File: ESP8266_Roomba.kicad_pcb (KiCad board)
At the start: 2 copper layers, 100 x 30 mm, 68 parts, among them P1 USB_OTG, P2 UG_62864, P3 CONN_01X04, P4 CONN_01X02, P5 CONN_01X07, P6 CONN_01X02, Q1 DMC204010R, Q2 2N7002, Q4 2N7002, Q5 2N7002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

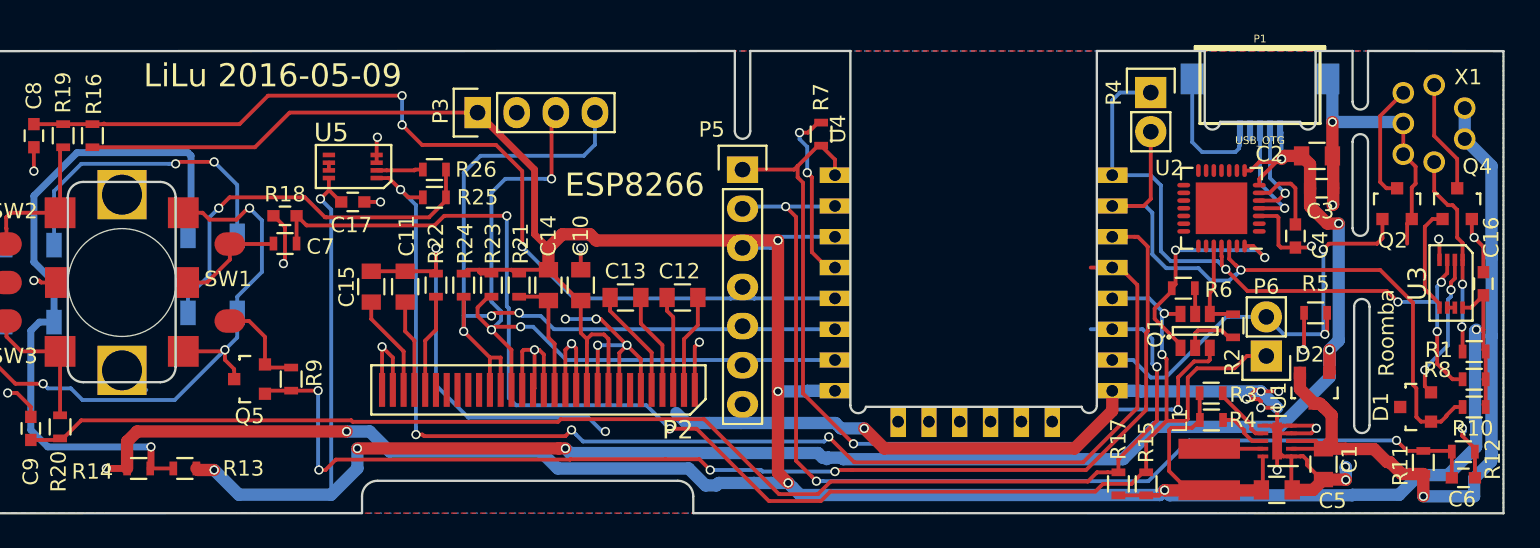
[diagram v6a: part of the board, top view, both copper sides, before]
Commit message: Revision 2 Fixed faulty footprint for diodes added partnumbers for more components calculated voltage devider for adc
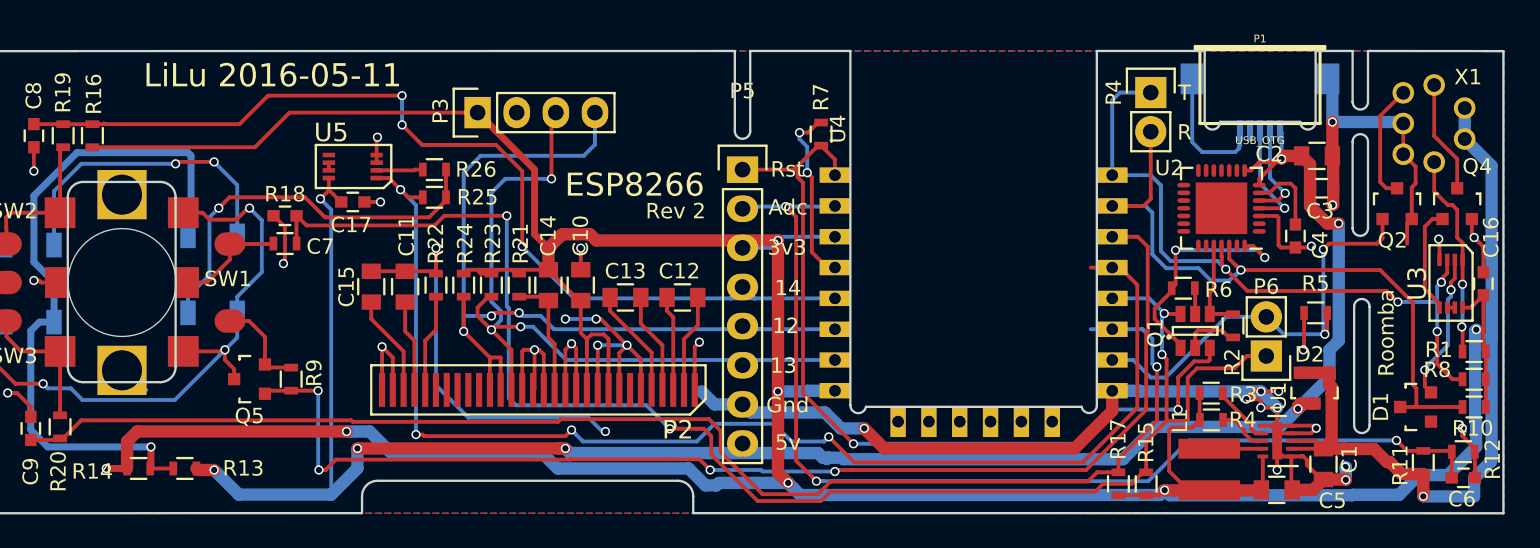
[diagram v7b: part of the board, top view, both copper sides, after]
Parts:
- D1, D2: value D_Schottky_x2_ACom_AKK -> MMBD717LT1G
- P5: value CONN_01X07 -> CONN_01X08; footprint Pin_Headers:Pin_Header_Straight_1x07 -> Pin_Headers:Pin_Header_Straight_1x08
- R11: value 100k -> 470k
- R12: value 100k -> 18k
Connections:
- D1 pad 1: /RXD -> (no net)
- D1 pad 3: (no net) -> /RXD
- D2 pad 1: /5V -> +12V
- D2 pad 3: +12V -> /5V
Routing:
- net GND: track 206.4 -> 204.1 mm
- net /LED: track 80.0 -> 81.0 mm
- net +12V: track 48.9 -> 49.8 mm
- net /Enc_A: track 87.8 -> 88.6 mm
- net /Switch: track 98.7 -> 99.4 mm
- net /5V: track 127.0 -> 127.6 mm
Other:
- board text added: "12"
- board text added: "13"
- board text added: "14"
- board text added: "3v3"
- board text added: "5v"
- board text added: "Adc"
- board text added: "Gnd"
- board text added: "LiLu 2016-05-11"
- board text added: "R"
- board text added: "Rev 2"
- board text added: "Rst"
- board text added: "T"
- board text removed: "LiLu 2016-05-09"

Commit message: Added output BOM with some links to digikey
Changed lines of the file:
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@@
     (links 183)
     (no_connects 3)
-    (area 99.884999 69.974999 200.035001 100.135001)
+    (area 99.3225 68.674001 201.6525 104.361666)
     (thickness 1.6)
     (drawings 60)
@@
   )
   (setup
-    (last_trace_width 0.8)
+    (last_trace_width 0.25)
     (user_trace_width 0.155)
     (user_trace_width 0.25)
@@
     (tags "resistor 0603")
     (attr smd)
-    (fp_text reference R18 (at 0 -3.2) (layer F.SilkS)
+    (fp_text reference R18 (at 2.7 0.18) (layer F.SilkS)
       (effects (font (size 1 1) (thickness 0.15)))
     )
@@
     (tags "capacitor 0603")
     (attr smd)
-    (fp_text reference C7 (at -2.3 -2 180) (layer F.SilkS)
-      (effects (font (size 1 1) (thickness 0.15)))
-    )
+    (fp_text reference C7 (at -0.03 1.42 180) (layer F.SilkS)
+      (effects (font (size 1 1) (thickness 0.15)))
+    )
